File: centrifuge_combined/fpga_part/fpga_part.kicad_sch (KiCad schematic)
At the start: 8 parts, among them X3 EC2620TTS-100.000MTR

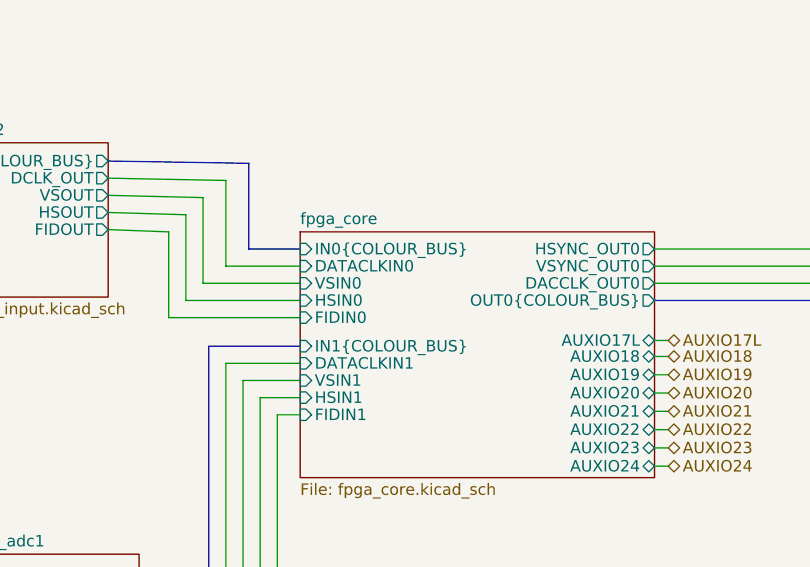
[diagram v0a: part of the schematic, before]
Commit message: fully commit to calling top VGA ADC2
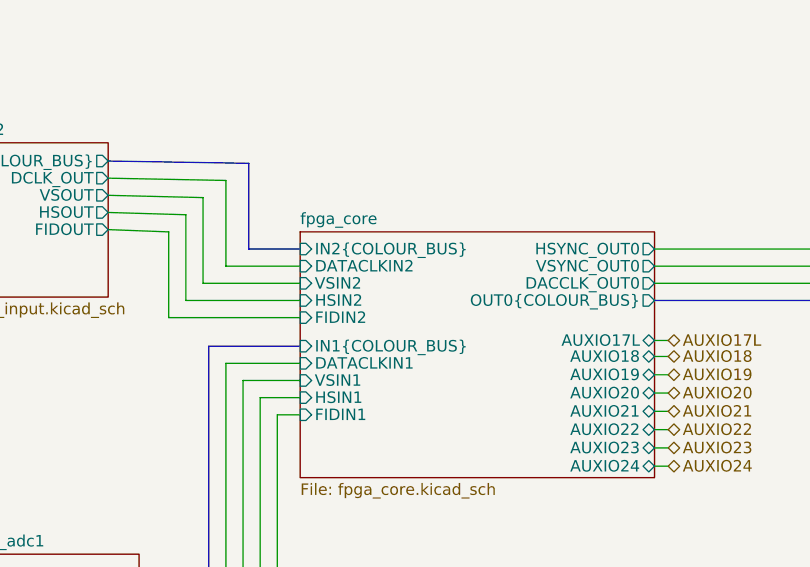
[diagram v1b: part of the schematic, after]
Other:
- sheet fpga_core ports: added DATACLKIN2, FIDIN2, HSIN2, IN2{COLOUR_BUS}, VSIN2; removed DATACLKIN0, FIDIN0, HSIN0, IN0{COLOUR_BUS}, VSIN0
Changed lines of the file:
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@@
       (effects (font (size 1.27 1.27)) (justify right))
     )
-    (pin "VSIN0" input (at 137.033 46.101 180)
+    (pin "VSIN2" input (at 137.033 46.101 180)
       (effects (font (size 1.27 1.27)) (justify left))
     )
-    (pin "HSIN0" input (at 137.033 48.006 180)
+    (pin "HSIN2" input (at 137.033 48.006 180)
       (effects (font (size 1.27 1.27)) (justify left))
     )
-    (pin "FIDIN0" input (at 137.033 49.911 180)
+    (pin "FIDIN2" input (at 137.033 49.911 180)
       (effects (font (size 1.27 1.27)) (justify left))
     )
@@
       (effects (font (size 1.27 1.27)) (justify left))
     )
-    (pin "DATACLKIN0" input (at 137.033 44.196 180)
+    (pin "DATACLKIN2" input (at 137.033 44.196 180)
       (effects (font (size 1.27 1.27)) (justify left))
     )
@@
       (effects (font (size 1.27 1.27)) (justify left))
     )
-    (pin "IN0{COLOUR_BUS}" input (at 137.033 42.291 180)
+    (pin "IN2{COLOUR_BUS}" input (at 137.033 42.291 180)
       (effects (font (size 1.27 1.27)) (justify left))
     )
